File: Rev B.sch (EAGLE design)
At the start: 37 parts

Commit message: Made some changes to the backlight circuit
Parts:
- removed JP_BKL: (no value), pinhead:PINHD-2X2
- added PRGHDR: (no value), pinhead:PINHD-1X3
- added Q1: BC817-25LT1SMD, transistor-npn:BC817-25LT1SMD
- added R9: 10kΩ, rcl:R-EU_R0805
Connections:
- removed net N$11: JP_BKL.3, LCD.A
- new net BKL_CTRL: MCU.4, R9.1
- new net N$16: Q1.B, R9.2
- new net RST: MCU.16, PRGHDR.3, R7.2
- new net TEST: MCU.17, PRGHDR.2
- net +5V: now also LCD.A; no longer JP_BKL.4
- net GND: now also PRGHDR.1, Q1.E; no longer LCD.K
- net N$9: now also LCD.K, Q1.C; no longer MCU.16, R7.2
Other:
- note added: "Change the 5V regulator to a LD1117"
- note added: "Change this pot to the SMD one"
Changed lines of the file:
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@@
 <setting verticaltext="up"/>
 </settings>
-<grid distance="0.1" unitdist="inch" unit="inch" style="lines" multiple="1" display="no" altdistance="0.01" altunitdist="inch" altunit="inch"/>
+<grid distance="0.05" unitdist="inch" unit="inch" style="lines" multiple="1" display="no" altdistance="0.01" altunitdist="inch" altunit="inch"/>
 <layers>
 <layer number="1" name="Top" color="4" fill="1" visible="no" active="no"/>
@@
 <part name="P+7" library="supply1" deviceset="VCC" device=""/>
 <part name="GND8" library="supply1" deviceset="GND" device=""/>
-<part name="JP_BKL" library="pinhead" deviceset="PINHD-2X2" device=""/>
 <part name="RE1" library="SparkFun-Electromechanical" deviceset="ROTARTY_ENCODER" device=""/>
 <part name="GND14" library="supply1" deviceset="GND" device=""/>
@@
 <part name="P+12" library="supply1" deviceset="VCC" device=""/>
 <part name="C8" library="SparkFun-Capacitors" deviceset="CAP_POL" device="1206" value="10uF"/>
+<part name="PRGHDR" library="pinhead" deviceset="PINHD-1X3" device=""/>
+<part name="GND22" library="supply1" deviceset="GND" device=""/>
+<part name="Q1" library="transistor-npn" deviceset="BC817*" device="SMD" technology="-25LT1"/>
+<part name="R9" library="rcl" deviceset="R-EU_" device="R0805" value="10kΩ"/>
 </parts>
 <sheets>
@@
 <text x="71.12" y="160.02" size="1.778" layer="91" rot="R90">Green 1206</text>
 <text x="262.89" y="-5.08" size="1.778" layer="91" rot="R180">MTP3055</text>
+<text x="-7.62" y="-2.54" size="5.08" layer="91" rot="R90">Change this pot to
+the SMD one</text>
+<text x="-7.62" y="86.36" size="1.778" layer="91" rot="R90">Change the 5V regulator to a LD1117</text>
 </plain>
 <instances>
@@
 <instance part="LCD" gate="G$1" x="81.28" y="20.32"/>
 <instance part="GND6" gate="1" x="60.96" y="20.32"/>
-<instance part="GND12" gate="1" x="60.96" y="-15.24"/>
+<instance part="GND12" gate="1" x="60.96" y="-26.67"/>
 <instance part="P+3" gate="VCC" x="195.58" y="185.42"/>
 <instance part="P+7" gate="VCC" x="252.73" y="204.47"/>
 <instance part="GND8" gate="1" x="10.16" y="15.24"/>
-<instance part="JP_BKL" gate="A" x="27.94" y="5.08"/>
 <instance part="RE1" gate="G$1" x="132.08" y="66.04" rot="R270"/>
 <instance part="GND14" gate="1" x="132.08" y="40.64"/>
@@
 <instance part="P+12" gate="VCC" x="107.95" y="85.09"/>
 <instance part="C8" gate="G$1" x="43.18" y="165.1"/>
+<instance part="PRGHDR" gate="A" x="137.16" y="158.75"/>
+<instance part="GND22" gate="1" x="125.73" y="143.51"/>
+<instance part="Q1" gate="G$1" x="58.42" y="-11.43"/>
+<instance part="R9" gate="G$1" x="40.64" y="-11.43"/>
 </instances>
 <busses>
@@
 <wire x1="71.12" y1="30.48" x2="60.96" y2="30.48" width="0.1524" layer="91"/>
 <junction x="60.96" y="30.48"/>
-</segment>
-<segment>
-<pinref part="LCD" gate="G$1" pin="K"/>
-<wire x1="71.12" y1="2.54" x2="60.96" y2="2.54" width="0.1524" layer="91"/>
-<wire x1="60.96" y1="2.54" x2="60.96" y2="-12.7" width="0.1524" layer="91"/>
-<pinref part="GND12" gate="1" pin="GND"/>
 </segment>
 <segment>
@@
 <pinref part="GND20" gate="1" pin="GND"/>
 </segment>
+<segment>
+<pinref part="PRGHDR" gate="A" pin="1"/>
+<wire x1="134.62" y1="161.29" x2="125.73" y2="161.29" width="0.1524" layer="91"/>
+<wire x1="125.73" y1="161.29" x2="125.73" y2="146.05" width="0.1524" layer="91"/>
+<pinref part="GND22" gate="1" pin="GND"/>
+</segment>
+<segment>
+<pinref part="GND12" gate="1" pin="GND"/>
+<wire x1="60.96" y1="-16.51" x2="60.96" y2="-24.13" width="0.1524" layer="91"/>
+<pinref part="Q1" gate="G$1" pin="E"/>
+</segment>
 </net>
 <net name="VCC" class="0">
@@
 </segment>
 </net>
-<net name="N$9" class="0">
+<net name="RST" class="0">
 <segment>
 <pinref part="MCU" gate="G$1" pin="16"/>
@@
 <wire x1="246.38" y1="154.94" x2="252.73" y2="154.94" width="0.1524" layer="91"/>
 <wire x1="252.73" y1="154.94" x2="252.73" y2="177.8" width="0.1524" layer="91"/>
+<junction x="252.73" y="154.94"/>
+<wire x1="252.73" y1="154.94" x2="261.62" y2="154.94" width="0.1524" layer="91"/>
+<label x="267.97" y="156.21" size="1.778" layer="95" rot="R180"/>
+</segment>
+<segment>
+<pinref part="PRGHDR" gate="A" pin="3"/>
+<wire x1="134.62" y1="156.21" x2="119.38" y2="156.21" width="0.1524" layer="91"/>
+<label x="119.38" y="157.48" size="1.778" layer="95" rot="R180"/>
 </segment>
 </net>
@@
 <wire x1="71.12" y1="35.56" x2="15.24" y2="35.56" width="0.1524" layer="91"/>
 <pinref part="VO" gate="G$1" pin="2"/>
-</segment>
-</net>
-<net name="N$11" class="0">
-<segment>
-<pinref part="LCD" gate="G$1" pin="A"/>
-<wire x1="71.12" y1="5.08" x2="40.64" y2="5.08" width="0.1524" layer="91"/>
-<wire x1="40.64" y1="5.08" x2="40.64" y2="0" width="0.1524" layer="91"/>
-<wire x1="40.64" y1="0" x2="15.24" y2="0" width="0.1524" layer="91"/>
-<wire x1="15.24" y1="0" x2="15.24" y2="5.08" width="0.1524" layer="91"/>
-<pinref part="JP_BKL" gate="A" pin="3"/>
-<wire x1="15.24" y1="5.08" x2="22.86" y2="5.08" width="0.1524" layer="91"/>
 </segment>
 </net>
@@
 <wire x1="10.16" y1="50.8" x2="38.1" y2="50.8" width="0.1524" layer="91"/>
 <junction x="38.1" y="50.8"/>
-<pinref part="JP_BKL" gate="A" pin="4"/>
-<wire x1="38.1" y1="5.08" x2="30.48" y2="5.08" width="0.1524" layer="91"/>
 <pinref part="VO" gate="G$1" pin="1"/>
 <pinref part="P+5" gate="1" pin="+5V"/>
+<pinref part="LCD" gate="G$1" pin="A"/>
+<wire x1="71.12" y1="5.08" x2="38.1" y2="5.08" width="0.1524" layer="91"/>
 </segment>
 <segment>
@@
 <wire x1="66.04" y1="38.1" x2="66.04" y2="58.42" width="0.1524" layer="91"/>
 <pinref part="P+6" gate="1" pin="+5V"/>
+</segment>
+</net>
+<net name="TEST" class="0">
+<segment>
+<pinref part="MCU" gate="G$1" pin="17"/>
+<wire x1="246.38" y1="157.48" x2="261.62" y2="157.48" width="0.1524" layer="91"/>
+<label x="269.24" y="158.75" size="1.778" layer="95" rot="R180"/>
+</segment>
+<segment>
+<pinref part="PRGHDR" gate="A" pin="2"/>
+<wire x1="134.62" y1="158.75" x2="119.38" y2="158.75" width="0.1524" layer="91"/>
+<label x="119.38" y="160.02" size="1.778" layer="95" rot="R180"/>
+</segment>
+</net>
+<net name="N$9" class="0">
+<segment>
+<pinref part="LCD" gate="G$1" pin="K"/>
+<wire x1="71.12" y1="2.54" x2="60.96" y2="2.54" width="0.1524" layer="91"/>
+<pinref part="Q1" gate="G$1" pin="C"/>
+<wire x1="60.96" y1="2.54" x2="60.96" y2="-6.35" width="0.1524" layer="91"/>
+</segment>
+</net>
+<net name="N$16" class="0">
+<segment>
+<pinref part="R9" gate="G$1" pin="2"/>
+<pinref part="Q1" gate="G$1" pin="B"/>
+<wire x1="45.72" y1="-11.43" x2="55.88" y2="-11.43" width="0.1524" layer="91"/>
+</segment>
+</net>
+<net name="BKL_CTRL" class="0">
+<segment>
+<pinref part="R9" gate="G$1" pin="1"/>
+<wire x1="35.56" y1="-11.43" x2="20.32" y2="-11.43" width="0.1524" layer="91"/>
+<label x="25.4" y="-8.89" size="1.778" layer="95" rot="R180"/>
+</segment>
+<segment>
+<pinref part="MCU" gate="G$1" pin="4"/>
+<wire x1="199.39" y1="157.48" x2="193.04" y2="157.48" width="0.1524" layer="91"/>
+<wire x1="193.04" y1="157.48" x2="193.04" y2="162.56" width="0.1524" layer="91"/>
+<wire x1="193.04" y1="162.56" x2="160.02" y2="162.56" width="0.1524" layer="91"/>
+<label x="168.91" y="165.1" size="1.778" layer="95" rot="R180"/>
 </segment>
 </net>
@@
 </schematic>
 </drawing>
+<compatibility>
+<note version="6.3" minversion="6.2.2" severity="warning">
+Since Version 6.2.2 text objects can contain more than one line,
+which will not be processed correctly with this version.
+</note>
+</compatibility>
 </eagle>

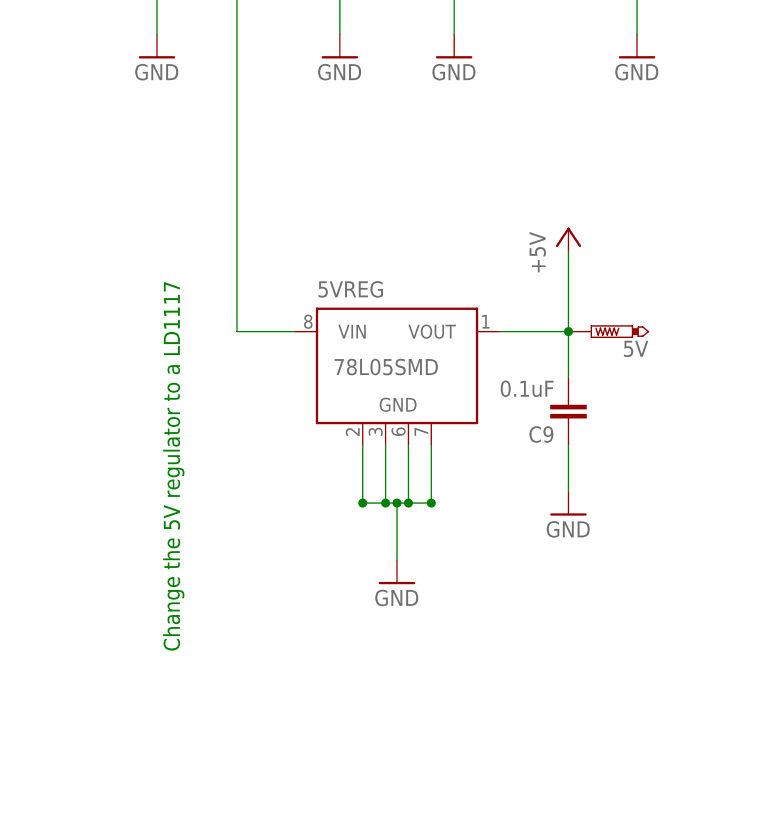
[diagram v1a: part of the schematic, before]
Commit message: Changed the 5V regulators
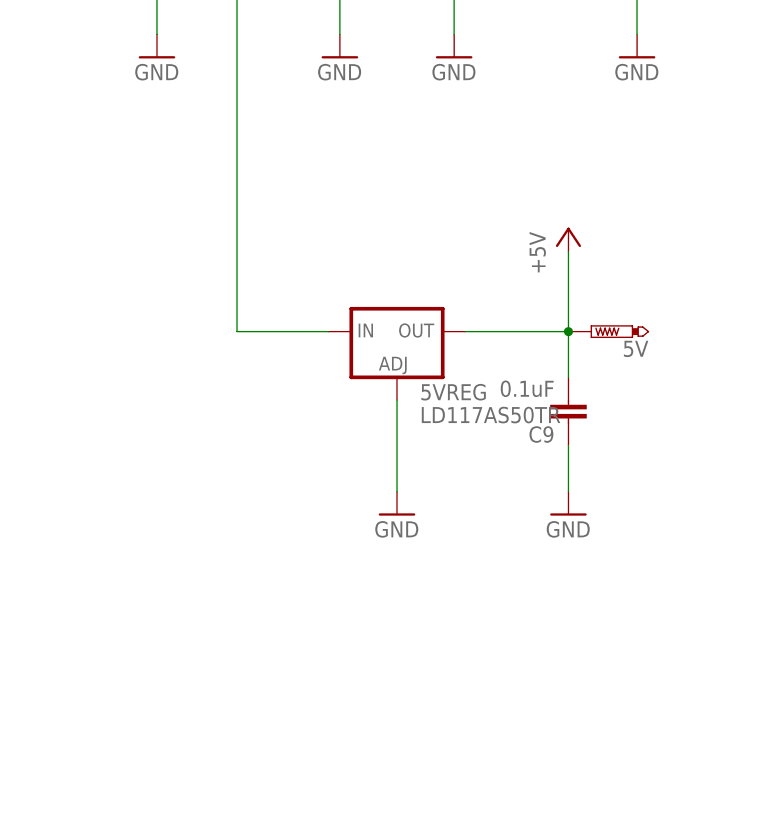
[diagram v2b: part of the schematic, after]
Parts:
- 5VREG: value 78L05SMD -> LD117AS50TR; device linear:78L05SMD -> v-reg:LD117AS50TR
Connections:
- net +5V: now also 5VREG.OUT; no longer 5VREGG$1.VOUT
- net GND: now also 5VREG.ADJ; no longer 5VREGG$1.GND@1, 5VREGG$1.GND@2, 5VREGG$1.GND@3, 5VREGG$1.GND@4
- net N$6: now also 5VREG.IN; no longer 5VREGG$1.VIN
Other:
- note removed: "Change the 5V regulator to a LD1117"
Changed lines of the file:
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@@
 <part name="GND19" library="supply1" deviceset="GND" device=""/>
 <part name="VO" library="bourns" deviceset="3386-" device="G" value="10kΩ"/>
-<part name="5VREG" library="linear" deviceset="78L*SMD" device="" technology="05"/>
 <part name="GND17" library="supply1" deviceset="GND" device=""/>
 <part name="P+10" library="supply1" deviceset="+5V" device=""/>
@@
 <part name="Q1" library="transistor-npn" deviceset="BC817*" device="SMD" technology="-25LT1"/>
 <part name="R9" library="rcl" deviceset="R-EU_" device="R0805" value="10kΩ"/>
+<part name="5VREG" library="v-reg" deviceset="LD117A?*" device="S" technology="50TR"/>
 </parts>
 <sheets>
@@
 <text x="-7.62" y="-2.54" size="5.08" layer="91" rot="R90">Change this pot to
 the SMD one</text>
-<text x="-7.62" y="86.36" size="1.778" layer="91" rot="R90">Change the 5V regulator to a LD1117</text>
 </plain>
 <instances>
@@
 <instance part="GND19" gate="1" x="148.59" y="73.66"/>
 <instance part="VO" gate="G$1" x="10.16" y="35.56" rot="MR180"/>
-<instance part="5VREG" gate="G$1" x="15.24" y="121.92"/>
-<instance part="GND17" gate="1" x="16.51" y="93.98"/>
+<instance part="GND17" gate="1" x="16.51" y="101.6"/>
 <instance part="P+10" gate="1" x="35.56" y="133.35"/>
 <instance part="P+5" gate="1" x="38.1" y="60.96"/>
@@
 <instance part="Q1" gate="G$1" x="58.42" y="-11.43"/>
 <instance part="R9" gate="G$1" x="40.64" y="-11.43"/>
+<instance part="5VREG" gate="G$1" x="16.51" y="121.92"/>
 </instances>
 <busses>
@@
 </segment>
 <segment>
-<pinref part="5VREG" gate="G$1" pin="GND@1"/>
-<wire x1="12.7" y1="109.22" x2="12.7" y2="102.87" width="0.1524" layer="91"/>
-<pinref part="5VREG" gate="G$1" pin="GND@4"/>
-<wire x1="12.7" y1="102.87" x2="15.24" y2="102.87" width="0.1524" layer="91"/>
-<wire x1="15.24" y1="102.87" x2="16.51" y2="102.87" width="0.1524" layer="91"/>
-<wire x1="16.51" y1="102.87" x2="17.78" y2="102.87" width="0.1524" layer="91"/>
-<wire x1="17.78" y1="102.87" x2="20.32" y2="102.87" width="0.1524" layer="91"/>
-<wire x1="20.32" y1="102.87" x2="20.32" y2="109.22" width="0.1524" layer="91"/>
-<pinref part="5VREG" gate="G$1" pin="GND@3"/>
-<wire x1="17.78" y1="109.22" x2="17.78" y2="102.87" width="0.1524" layer="91"/>
-<pinref part="5VREG" gate="G$1" pin="GND@2"/>
-<wire x1="15.24" y1="109.22" x2="15.24" y2="102.87" width="0.1524" layer="91"/>
-<junction x="15.24" y="102.87"/>
-<junction x="17.78" y="102.87"/>
-<junction x="12.7" y="102.87"/>
-<junction x="20.32" y="102.87"/>
-<wire x1="16.51" y1="102.87" x2="16.51" y2="96.52" width="0.1524" layer="91"/>
+<wire x1="16.51" y1="114.3" x2="16.51" y2="104.14" width="0.1524" layer="91"/>
 <pinref part="GND17" gate="1" pin="GND"/>
-<junction x="16.51" y="102.87"/>
+<pinref part="5VREG" gate="G$1" pin="ADJ"/>
 </segment>
 <segment>
@@
 <pinref part="PWR" gate="G$1" pin="2"/>
 <wire x1="-1.27" y1="172.72" x2="-1.27" y2="121.92" width="0.1524" layer="91"/>
-<pinref part="5VREG" gate="G$1" pin="VIN"/>
-<wire x1="-1.27" y1="121.92" x2="5.08" y2="121.92" width="0.1524" layer="91"/>
+<wire x1="-1.27" y1="121.92" x2="8.89" y2="121.92" width="0.1524" layer="91"/>
 <junction x="-1.27" y="172.72"/>
+<pinref part="5VREG" gate="G$1" pin="IN"/>
 </segment>
 </net>
@@
 <net name="+5V" class="0">
 <segment>
-<pinref part="5VREG" gate="G$1" pin="VOUT"/>
 <pinref part="P+10" gate="1" pin="+5V"/>
-<wire x1="27.94" y1="121.92" x2="35.56" y2="121.92" width="0.1524" layer="91"/>
+<wire x1="24.13" y1="121.92" x2="35.56" y2="121.92" width="0.1524" layer="91"/>
 <wire x1="35.56" y1="121.92" x2="35.56" y2="130.81" width="0.1524" layer="91"/>
 <pinref part="C9" gate="G$1" pin="2"/>
@@
 <junction x="35.56" y="121.92"/>
 <pinref part="5V" gate="G$1" pin="TP"/>
-</segment>
-<segment>
+<pinref part="5VREG" gate="G$1" pin="OUT"/>
+</segment>
+<segment>

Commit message: Final design
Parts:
- removed VO: 10kΩ, bourns:3386-G
- added R10: TRIMPOT-2, SparkFun-Electromechanical:TRIMPOT-2
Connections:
- net +5V: now also R10.CCW; no longer VO.1
- net GND: now also R10.CW; no longer VO.3
- net N$10: now also R10.WIPER; no longer VO.2
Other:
- note added: "10kΩ"
- note removed: "Change this pot to the SMD one"
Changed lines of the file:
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@@
 <part name="R8" library="rcl" deviceset="R-EU_" device="R0805" value="10kΩ"/>
 <part name="GND19" library="supply1" deviceset="GND" device=""/>
-<part name="VO" library="bourns" deviceset="3386-" device="G" value="10kΩ"/>
 <part name="GND17" library="supply1" deviceset="GND" device=""/>
 <part name="P+10" library="supply1" deviceset="+5V" device=""/>
@@
 <part name="R9" library="rcl" deviceset="R-EU_" device="R0805" value="10kΩ"/>
 <part name="5VREG" library="v-reg" deviceset="LD117A?*" device="S" technology="50TR"/>
+<part name="R10" library="SparkFun-Electromechanical" deviceset="TRIMPOT" device="-2"/>
 </parts>
 <sheets>
@@
 <text x="71.12" y="160.02" size="1.778" layer="91" rot="R90">Green 1206</text>
 <text x="262.89" y="-5.08" size="1.778" layer="91" rot="R180">MTP3055</text>
-<text x="-7.62" y="-2.54" size="5.08" layer="91" rot="R90">Change this pot to
-the SMD one</text>
+<text x="5.08" y="33.02" size="1.778" layer="91" rot="R90">10kΩ</text>
 </plain>
 <instances>
@@
 <instance part="R8" gate="G$1" x="134.62" y="90.17"/>
 <instance part="GND19" gate="1" x="148.59" y="73.66"/>
-<instance part="VO" gate="G$1" x="10.16" y="35.56" rot="MR180"/>
 <instance part="GND17" gate="1" x="16.51" y="101.6"/>
 <instance part="P+10" gate="1" x="35.56" y="133.35"/>
@@
 <instance part="R9" gate="G$1" x="40.64" y="-11.43"/>
 <instance part="5VREG" gate="G$1" x="16.51" y="121.92"/>
+<instance part="R10" gate="R?" x="10.16" y="35.56" smashed="yes" rot="R270">
+<attribute name="NAME" x="6.35" y="38.1" size="1.778" layer="95" rot="R270"/>
+<attribute name="VALUE" x="11.43" y="36.068" size="1.778" layer="96"/>
+</instance>
 </instances>
 <busses>
@@
 <wire x1="10.16" y1="30.48" x2="10.16" y2="17.78" width="0.1524" layer="91"/>
 <pinref part="GND8" gate="1" pin="GND"/>
-<pinref part="VO" gate="G$1" pin="3"/>
+<pinref part="R10" gate="R?" pin="CW"/>
 </segment>
 <segment>
@@
 <pinref part="LCD" gate="G$1" pin="VO"/>
 <wire x1="71.12" y1="35.56" x2="15.24" y2="35.56" width="0.1524" layer="91"/>
-<pinref part="VO" gate="G$1" pin="2"/>
+<pinref part="R10" gate="R?" pin="WIPER"/>
 </segment>
 </net>
@@
 <wire x1="10.16" y1="50.8" x2="38.1" y2="50.8" width="0.1524" layer="91"/>
 <junction x="38.1" y="50.8"/>
-<pinref part="VO" gate="G$1" pin="1"/>
 <pinref part="P+5" gate="1" pin="+5V"/>
 <pinref part="LCD" gate="G$1" pin="A"/>
 <wire x1="71.12" y1="5.08" x2="38.1" y2="5.08" width="0.1524" layer="91"/>
+<pinref part="R10" gate="R?" pin="CCW"/>
 </segment>
 <segment>
@@
 </schematic>
 </drawing>
-<compatibility>
-<note version="6.3" minversion="6.2.2" severity="warning">
-Since Version 6.2.2 text objects can contain more than one line,
-which will not be processed correctly with this version.
-</note>
-</compatibility>
 </eagle>

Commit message: Finished Rev B
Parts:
- removed C6: 0.1uF, rcl:C-EUC0805
- removed IV, IVO, SGND: PTR1TP10SQ, testpad:PTR1TP10SQ
- removed OP2: TLV2372IP, Texas Instruments_By_element14_Batch_1:TLV2372IP
- removed SHUNT: 1Ω, rcl:R-EU_VTA52
- added R11, R12, R13, R14, R15, R16, R17, R18: 10Ω, rcl:R-EU_R2512
- added VO: TRIMPOT-2, SparkFun-Electromechanical:TRIMPOT-2
- C5: value 0.1uF -> 1uF
- R10: value TRIMPOT-2 -> 10Ω; device SparkFun-Electromechanical:TRIMPOT-2 -> rcl:R-EU_R2512
- R2: value 1kΩ -> 10Ω; device rcl:R-EU_R0805 -> rcl:R-EU_R2512
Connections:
- removed net N$1: C2.2, OP1.2IN-, OP2.1IN_+, R2.1
- removed net N$13: IV.TP, N-CHANNEL.S, R2.2, SHUNT.2
- net +5V: now also VO.CCW; no longer R10.CCW
- net CURR_SENSE: now also C2.2, N-CHANNEL.S, OP1.2IN-, R10.2, R11.2, R12.2, R13.2, R14.2, R15.2, R16.2, R17.2, R18.2, R2.2; no longer IVO.TP, OP2.1IN-, OP2.1OUT
- net GND: now also R10.1, R11.1, R12.1, R13.1, R14.1, R15.1, R16.1, R17.1, R18.1, R2.1, VO.CW; no longer C6.1, OP2.GND, R10.CW, SGND.TP, SHUNT.1
- net N$10: now also VO.WIPER; no longer R10.WIPER
- net VCC: no longer C6.2, OP2.VDD
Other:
- moved on the sheet: R2

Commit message: Finished Rev B
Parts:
- removed 3VREG: LD117AS33TR, v-reg:LD117AS33TR
- removed 5VREG: LD117AS50TR, v-reg:LD117AS50TR
- removed GND: PTR1TP10SQ, testpad:PTR1TP10SQ
- removed R16, R17, R18: 10Ω, rcl:R-EU_R2512
- added C10: 10nF, rcl:C-EU050-025X075
- added C6: 0.1uF, rcl:C-EU050-025X075
- added C7: 1uF, rcl:C-EU025-025X050
- 3V3, 5V: value PTR1TP10SQ -> 7805TV; device testpad:PTR1TP10SQ -> linear:7805TV
- C1: value 0.1uF -> 2.2uF; device rcl:C-EUC0805 -> rcl:CPOL-EUE2.5-6
- C2: value 10nF -> 2.2uF; device rcl:C-EUC0805 -> rcl:CPOL-EUE2.5-6
- C3: value 0.1uF -> 47uF; device rcl:C-EUC0805 -> rcl:CPOL-EUE2.5-6
- C4: value 0.1uF -> 22uF; device rcl:C-EUC0805 -> rcl:CPOL-EUE2.5-6
- C5: value 1uF -> 10nF; device rcl:C-EUC0805 -> rcl:C-EU050-025X075
- C8: value 10uF -> 0.1uF; device SparkFun-Capacitors:CAP_POL1206 -> rcl:C-EU050-025X075
- C9: value 0.1uF -> 10nF; device rcl:C-EUC0805 -> rcl:C-EU050-025X075
- ON: device led:LEDCHIPLED_1206 -> led:LEDSQR2X5
- Q1: value BC817-25LT1SMD -> BC547; device transistor-npn:BC817-25LT1SMD -> transistor-npn:BC547
- R1, R5: device rcl:R-EU_R0805 -> resistor:R-EU_0207/10
- R10, R12, R13, R14, R15: value 10Ω -> 5Ω; device rcl:R-EU_R2512 -> rcl:R-EU_0613/15
- R11: value 10Ω -> 10kΩ; device rcl:R-EU_R2512 -> resistor:R-EU_0207/10
- R2: value 10Ω -> 1kΩ; device rcl:R-EU_R2512 -> resistor:R-EU_0207/10
- R3, R4: value 1kΩ -> 10kΩ; device rcl:R-EU_R0805 -> resistor:R-EU_0207/10
- R6: value 100kΩ -> 10kΩ; device rcl:R-EU_R0805 -> resistor:R-EU_0207/10
- R7: device resistor:R-EU_R0805 -> resistor:R-EU_0207/10
- R8: value 10kΩ -> 100kΩ; device rcl:R-EU_R0805 -> resistor:R-EU_0207/10
- R9: value 10kΩ -> 1kΩ; device rcl:R-EU_R0805 -> resistor:R-EU_0207/10
- VO: value TRIMPOT-2 -> 10kΩ; device SparkFun-Electromechanical:TRIMPOT-2 -> bourns:3362H
- renumbered PWR_IN to TEST_IN
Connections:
- removed net N$7: ON.C, R4.2
- new net RE_A_: R3.2, R4.1, RE1.A
- new net RE_B_: R6.1, R7.1, RE1.B
- new net VIN: 3V3.VI, 5V.VI, C1.+, C2.+, ON.A, PWR.2
- net +5V: now also 5V.VO, C4.+, VO.3; no longer 5V.TP, 5VREG.OUT, C9.2, VO.CCW
- net BKL_CTRL: now also R1.1; no longer R9.1
- net CURR_SENSE: now also C10.2; no longer C2.2, R11.2, R16.2, R17.2, R18.2, R2.2
- net GND: now also 3V3.GND, 5V.GND, C1.-, C2.-, C3.-, C4.-, C5.2, C6.1, C7.2, C8.1, C9.2, VO.1; no longer 3VREG.ADJ, 5VREG.ADJ, C1.1, C3.1, C4.1, C5.1, C8.-, C9.1, GND.TP, R11.1, R16.1, R17.1, R18.1, R4.1, VO.CW
- net N$10: now also VO.2; no longer VO.WIPER
- net N$16: now also R1.2; no longer R9.2
- net N$3: now also R9.2; no longer R3.2
- net N$4: now also C10.1, R9.1; no longer C2.1, R3.1
- net N$6: now also ON.C, R2.2; no longer 3VREG.IN, 5VREG.IN, C3.2, PWR.2
- net N$8: now also R8.2; no longer R6.2
- net PWM_FILTERED: now also C7.1, R8.1; no longer C5.2, R6.1
- net RE_A: now also C5.1, R3.1; no longer R5.1, RE1.A
- net RE_B: now also C9.1, R7.2; no longer R1.1, RE1.B
- net RE_BTN: now also R5.1; no longer R8.1
- net RST: now also R11.1; no longer R7.2
- net VCC: now also 3V3.VO, C3.+, C6.2, C8.2, R11.2, R4.2, R6.2; no longer 3V3.TP, 3VREG.OUT, C1.2, C4.2, C8.+, ON.A, R1.2, R7.1, R8.2
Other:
- note added: "TC1262"
- note removed: "10kΩ"
- note removed: "Green 1206"
- moved on the sheet: C5, C9, HEATSINK, LCD, N-CHANNEL, ON, Q1, R1, R10, R11, R12, R13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
